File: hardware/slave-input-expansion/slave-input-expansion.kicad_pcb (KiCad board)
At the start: 2 copper layers, 78 parts, among them J1 Screw_Terminal_01x02, J10 Screw_Terminal_01x02, J11 Conn_01x06, J12 ICSP, J2 Screw_Terminal_01x02, J3 Screw_Terminal_01x02, J4 Screw_Terminal_01x02, J5 Screw_Terminal_01x02, J6 Screw_Terminal_01x02, J7 Screw_Terminal_01x02, J8 Screw_Terminal_01x02, J9 Conn_02x06_Odd_Even, SW1 SW_Push, SW2 SW_Push, U1 PC817XI, U10 DS1233A-10, U11 ESP32, U12 LM2596S-3.3, U13 LM2596S-3.3, U14 AMS1117-5.0, U2 PC817XI, U3 PC817XI, U4 PC817XI, U5 PC817XI, U6 PC817XI, U7 PC817XI, U8 PC817XI, U9 PCF8574

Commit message: Diseño mecanico del ensamblaje
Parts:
- removed C2, C4, C5: 100nF, Capacitor_SMD:C_1206_3216Metric_Pad1.33x1.80mm_HandSolder
- removed C3: 1uF, Capacitor_SMD:C_1206_3216Metric_Pad1.33x1.80mm_HandSolder
- removed C6, C7: 470uF, libs:CAP_10x10_SMD_THT
- removed D1: ABS10, Diode_SMD:Diode_Bridge_Diotec_ABS
- removed D2: LED, LED_SMD:LED_1206_3216Metric
- removed D3, D4: SS14, Diode_SMD:D_SMA_Handsoldering
- removed JP1, JP10, JP11, JP2, JP3, JP4, JP5, JP6, JP7, JP8, JP9: SolderJumper_2_Open, Jumper:SolderJumper-2_P1.3mm_Open_RoundedPad1.0x1.5mm
- removed L1, L2: 68uH, libs:L_12x12mm_H8mm
- removed R10, R11, R12, R13, R14, R15, R16, R17, R18, R19, R20, R21, R22, R23, R24, R9: 10k, Resistor_SMD:R_1206_3216Metric
- removed R25: 4K7, Resistor_SMD:R_1206_3216Metric
- removed R26: 5.6K, Resistor_THT:R_Axial_DIN0204_L3.6mm_D1.6mm_P2.54mm_Vertical
- removed R27: 12K, Resistor_THT:R_Axial_DIN0204_L3.6mm_D1.6mm_P2.54mm_Vertical
- removed SW1, SW2: SW_Push, Button_Switch_THT:SW_PUSH_6mm
- removed U10: DS1233A-10, Package_TO_SOT_THT:TO-92
- removed U12, U13: LM2596S-3.3, libs:TO-263-5_TabPin3
- removed U14: AMS1117-5.0, Package_TO_SOT_SMD:SOT-223-3_TabPin2
- removed U9: PCF8574, Package_SO:SOIC-16W_7.5x10.3mm_P1.27mm
- moved J11 84.2 mm to (181.6, 124.5)
- moved U11 81.8 mm to (184.2, 109.2), turned to -90 degrees
- moved J12 78.8 mm to (164.3, 124.5), turned to 90 degrees
- moved locked 69.0 mm to (188.0, 91.4), turned to 180 degrees
- moved R3 65.7 mm to (137.2, 97.8), turned to 180 degrees
- moved U3 65.1 mm to (124.5, 105.4), turned to -90 degrees
- moved locked 54.1 mm to (116.8, 91.4), turned to 180 degrees
- moved R1 53.4 mm to (116.8, 97.8), turned to 180 degrees
- moved R8 51.5 mm to (188.0, 97.8), turned to 180 degrees
- moved R7 50.2 mm to (177.8, 97.8), turned to 180 degrees
- moved locked 50.0 mm to (177.8, 91.4), turned to 180 degrees
- moved U7 49.7 mm to (149.9, 105.4), turned to -90 degrees
- moved J9 47.9 mm to (139.2, 116.8), turned to 90 degrees
- moved U8 46.3 mm to (156.2, 105.4), turned to -90 degrees
- moved U6 44.1 mm to (143.5, 105.4), turned to -90 degrees
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- renumbered J8 to locked, J1 to locked, J4 to locked, J2 to locked, J7 to locked, J5 to locked, J3 to locked, J6 to locked
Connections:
- R1 pad 2: Net-(J1-Pad1) -> Net-(R1-Pad2)
- R2 pad 2: Net-(J2-Pad1) -> Net-(R2-Pad2)
- R3 pad 2: Net-(J3-Pad1) -> Net-(R3-Pad2)
- R4 pad 2: Net-(J4-Pad1) -> Net-(R4-Pad2)
- R5 pad 2: Net-(J5-Pad1) -> Net-(R5-Pad2)
- R6 pad 2: Net-(J6-Pad1) -> Net-(J6-Pad2)
- R7 pad 2: Net-(J7-Pad1) -> Net-(R7-Pad2)
- R8 pad 2: Net-(J8-Pad1) -> Net-(R8-Pad2)
- U1 pad 2: Net-(J1-Pad2) -> Net-(U1-Pad2)
- U2 pad 2: Net-(J2-Pad2) -> Net-(U2-Pad2)
- U3 pad 2: Net-(J3-Pad2) -> Net-(U3-Pad2)
- U4 pad 2: Net-(J4-Pad2) -> Net-(U4-Pad2)
- U5 pad 2: Net-(J5-Pad2) -> Net-(U5-Pad2)
- U6 pad 2: Net-(J6-Pad2) -> Net-(U6-Pad2)
- U7 pad 2: Net-(J7-Pad2) -> Net-(U7-Pad2)
- U8 pad 2: Net-(J8-Pad2) -> Net-(U8-Pad2)
- locked pad 1: Net-(J8-Pad1) -> Net-(U8-Pad2)
- locked pad 2: Net-(J8-Pad2) -> Net-(R8-Pad2)
- locked pad 1: Net-(J1-Pad1) -> Net-(U1-Pad2)
- locked pad 2: Net-(J1-Pad2) -> Net-(R1-Pad2)
- locked pad 1: Net-(J4-Pad1) -> Net-(U4-Pad2)
- locked pad 2: Net-(J4-Pad2) -> Net-(R4-Pad2)
- locked pad 1: Net-(J2-Pad1) -> Net-(U2-Pad2)
- locked pad 2: Net-(J2-Pad2) -> Net-(R2-Pad2)
- locked pad 1: Net-(J7-Pad1) -> Net-(U7-Pad2)
- locked pad 2: Net-(J7-Pad2) -> Net-(R7-Pad2)
- locked pad 1: Net-(J5-Pad1) -> Net-(U5-Pad2)
- locked pad 2: Net-(J5-Pad2) -> Net-(R5-Pad2)
- locked pad 1: Net-(J3-Pad1) -> Net-(U3-Pad2)
- locked pad 2: Net-(J3-Pad2) -> Net-(R3-Pad2)
- locked pad 1: Net-(J6-Pad1) -> Net-(U6-Pad2)
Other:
- board outline added: 100 x 43 mm

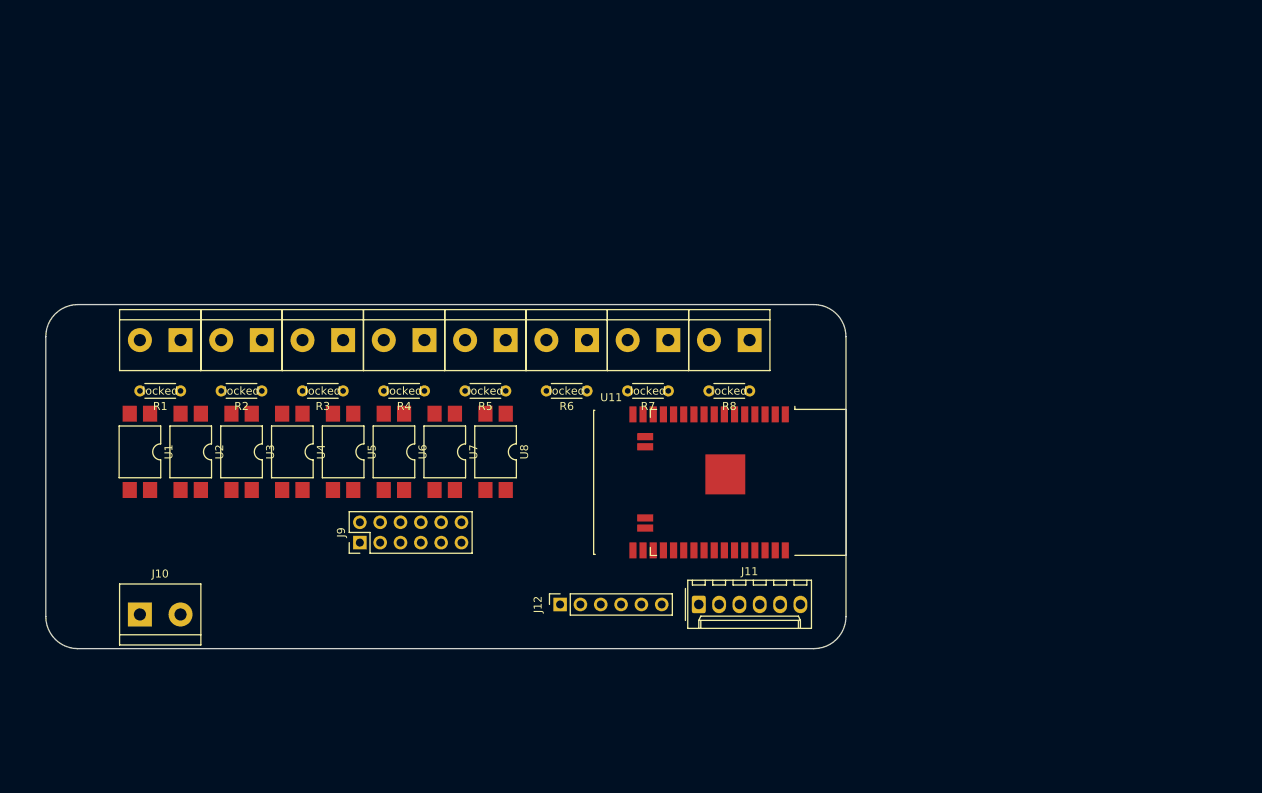
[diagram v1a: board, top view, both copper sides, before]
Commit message: Routeo de la placa expansion
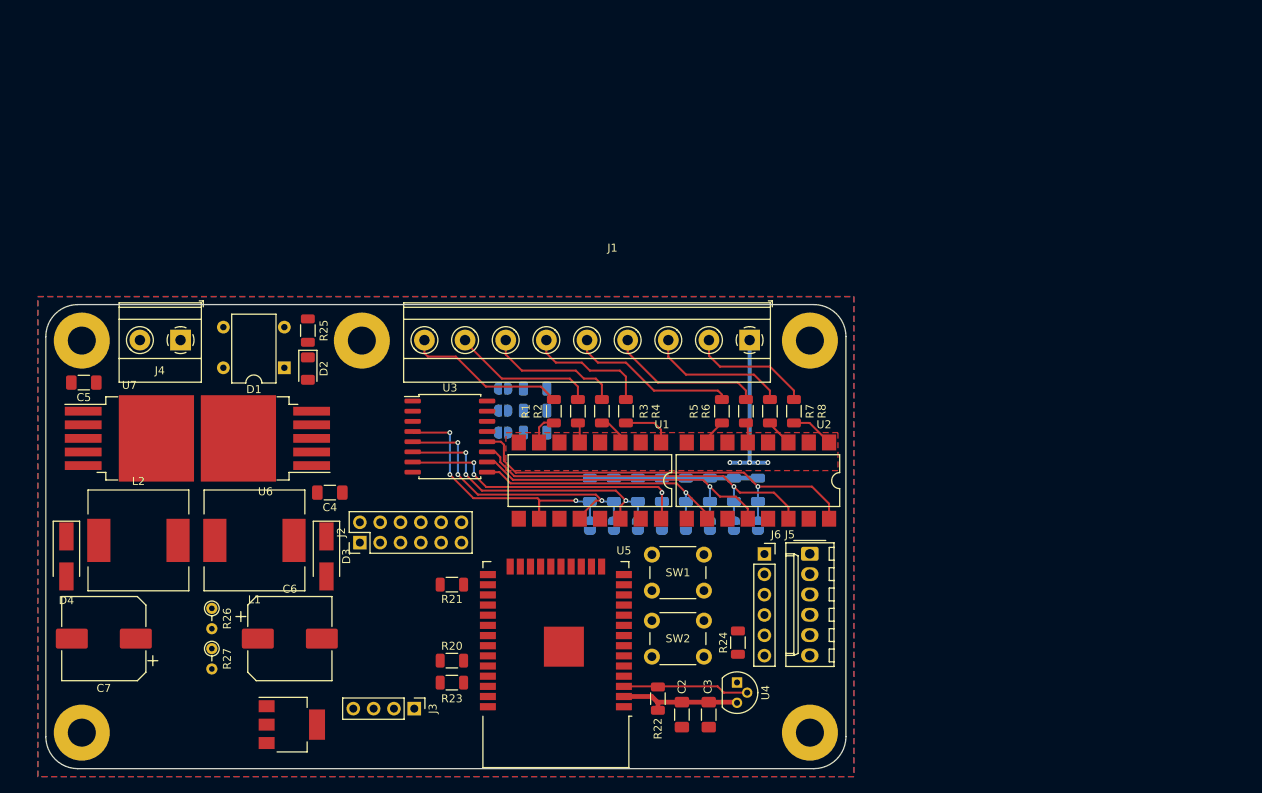
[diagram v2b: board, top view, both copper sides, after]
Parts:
- removed the U5 at (137.2, 105.4)
- removed locked (x8): Screw_Terminal_01x02, libs:TerminalBlock_bornier-2_P5.08mm
- added ?: , , F.Cu at (195.5, 140.5)
- added ?: , , F.Cu at (139.5, 91.5)
- added ?: , , F.Cu at (104.5, 91.5)
- added ?: , , F.Cu at (104.5, 140.5)
- added C2: 100nF, Capacitor_SMD:C_1206_3216Metric_Pad1.33x1.80mm_HandSolder, F.Cu at (179.5, 138.2)
- added C3: 1uF, Capacitor_SMD:C_1206_3216Metric_Pad1.33x1.80mm_HandSolder, F.Cu at (182.8, 138.2)
- added C4: 100nF, Capacitor_SMD:C_1206_3216Metric_Pad1.33x1.80mm_HandSolder, F.Cu at (135.5, 110.5)
- added C5: 100nF, Capacitor_SMD:C_1206_3216Metric_Pad1.33x1.80mm_HandSolder, F.Cu at (104.8, 96.8)
- added C6: 470uF, Capacitor_SMD:CP_Elec_10x10, F.Cu at (130.5, 128.8)
- added C7: 470uF, Capacitor_SMD:CP_Elec_10x10, F.Cu at (107.2, 128.8)
- added D1: DB157, Diode_THT:Diode_Bridge_DIP-4_W7.62mm_P5.08mm, F.Cu at (129.8, 94.9)
- added D2: LED, LED_SMD:LED_1206_3216Metric, F.Cu at (132.8, 95.0)
- added D3: SS14, Diode_SMD:D_SMA_Handsoldering, F.Cu at (135.1, 118.5)
- added D4: SS14, Diode_SMD:D_SMA_Handsoldering, F.Cu at (102.6, 118.5)
- added J1: Screw_Terminal_01x09, TerminalBlock_Phoenix:TerminalBlock_Phoenix_MKDS-1,5-9-5.08_1x09_P5.08mm_Horizontal, F.Cu at (188.0, 91.4)
- added J3: Conn_01x04, Connector_PinHeader_2.54mm:PinHeader_1x04_P2.54mm_Vertical, F.Cu at (146.1, 137.5)
- added JP1: SolderJumper_2_Open, Jumper:SolderJumper-2_P1.3mm_Open_RoundedPad1.0x1.5mm, B.Cu at (168.0, 114.7)
- added JP10: SolderJumper_2_Open, Jumper:SolderJumper-2_P1.3mm_Open_RoundedPad1.0x1.5mm, B.Cu at (157.2, 100.2)
- added JP11: SolderJumper_2_Open, Jumper:SolderJumper-2_P1.3mm_Open_RoundedPad1.0x1.5mm, B.Cu at (157.2, 103.0)
- added JP2: SolderJumper_2_Open, Jumper:SolderJumper-2_P1.3mm_Open_RoundedPad1.0x1.5mm, B.Cu at (171.0, 114.7)
- added JP3: SolderJumper_2_Open, Jumper:SolderJumper-2_P1.3mm_Open_RoundedPad1.0x1.5mm, B.Cu at (174.0, 114.7)
- added JP4: SolderJumper_2_Open, Jumper:SolderJumper-2_P1.3mm_Open_RoundedPad1.0x1.5mm, B.Cu at (177.0, 114.7)
- added JP5: SolderJumper_2_Open, Jumper:SolderJumper-2_P1.3mm_Open_RoundedPad1.0x1.5mm, B.Cu at (180.0, 114.7)
- added JP6: SolderJumper_2_Open, Jumper:SolderJumper-2_P1.3mm_Open_RoundedPad1.0x1.5mm, B.Cu at (183.0, 114.7)
- added JP7: SolderJumper_2_Open, Jumper:SolderJumper-2_P1.3mm_Open_RoundedPad1.0x1.5mm, B.Cu at (186.0, 114.7)
- added JP8: SolderJumper_2_Open, Jumper:SolderJumper-2_P1.3mm_Open_RoundedPad1.0x1.5mm, B.Cu at (189.0, 114.7)
- added JP9: SolderJumper_2_Open, Jumper:SolderJumper-2_P1.3mm_Open_RoundedPad1.0x1.5mm, B.Cu at (157.2, 97.5)
- added L1: 68uH, Inductor_SMD:L_12x12mm_H8mm, F.Cu at (126.1, 116.5)
- added L2: 68uH, Inductor_SMD:L_12x12mm_H8mm, F.Cu at (111.6, 116.5)
- added R10: 10k, Resistor_SMD:R_1206_3216Metric, B.Cu at (171.0, 110.2)
- added R11: 10k, Resistor_SMD:R_1206_3216Metric, B.Cu at (174.0, 110.2)
- added R12: 10k, Resistor_SMD:R_1206_3216Metric, B.Cu at (177.0, 110.2)
- added R13: 10k, Resistor_SMD:R_1206_3216Metric, B.Cu at (180.0, 110.2)
- added R14: 10k, Resistor_SMD:R_1206_3216Metric, B.Cu at (183.0, 110.2)
- added R15: 10k, Resistor_SMD:R_1206_3216Metric, B.Cu at (186.0, 110.2)
- added R16: 10k, Resistor_SMD:R_1206_3216Metric, B.Cu at (189.0, 110.2)
- added R17: 10k, Resistor_SMD:R_1206_3216Metric, B.Cu at (161.2, 103.0)
- added R18: 10k, Resistor_SMD:R_1206_3216Metric, B.Cu at (161.2, 100.2)
- added R19: 10k, Resistor_SMD:R_1206_3216Metric, B.Cu at (161.2, 97.5)
- added R20: 10k, Resistor_SMD:R_1206_3216Metric, F.Cu at (150.8, 131.5)
- added R21: 10k, Resistor_SMD:R_1206_3216Metric, F.Cu at (150.8, 122.0)
- added R22: 10k, Resistor_SMD:R_1206_3216Metric, F.Cu at (176.5, 136.2)
- added R23: 10k, Resistor_SMD:R_1206_3216Metric, F.Cu at (150.8, 134.2)
- added R24: 10k, Resistor_SMD:R_1206_3216Metric, F.Cu at (186.5, 129.2)
- added R25: 4K7, Resistor_SMD:R_1206_3216Metric, F.Cu at (132.8, 90.2)
- added R26: 5.6K, Resistor_THT:R_Axial_DIN0204_L3.6mm_D1.6mm_P2.54mm_Vertical, F.Cu at (120.8, 125.0)
- added R27: 12K, Resistor_THT:R_Axial_DIN0204_L3.6mm_D1.6mm_P2.54mm_Vertical, F.Cu at (120.8, 130.0)
- added R9: 10k, Resistor_SMD:R_1206_3216Metric, B.Cu at (168.0, 110.2)
- added REF**: MountingHole_3.5mm_Pad, MountingHole:MountingHole_3.5mm_Pad, F.Cu at (195.5, 91.5)
- added SW1: SW_Push, Button_Switch_THT:SW_PUSH_6mm, F.Cu at (182.2, 122.8)
- added SW2: SW_Push, Button_Switch_THT:SW_PUSH_6mm, F.Cu at (182.2, 131.0)
- J4: renamed from J10; footprint libs:TerminalBlock_bornier-2_P5.08mm -> TerminalBlock_Phoenix:TerminalBlock_Phoenix_MKDS-1,5-2-5.08_1x02_P5.08mm_Horizontal
- R1, R2, R3, R4, R5, R6, R7, R8: value 2.2k -> 1k; footprint Resistor_THT:R_Axial_DIN0204_L3.6mm_D1.6mm_P5.08mm_Horizontal -> Resistor_SMD:R_1206_3216Metric
- U1, U2: value PC817XI -> LTV-847S; footprint Package_DIP:SMDIP-4_W9.53mm -> Package_DIP:SMDIP-16_W9.53mm
- U3: value PC817XI -> PCF8574; footprint Package_DIP:SMDIP-4_W9.53mm -> Package_SO:SOIC-16W_7.5x10.3mm_P1.27mm
- U4: value PC817XI -> DS1233A-10; footprint Package_DIP:SMDIP-4_W9.53mm -> Package_TO_SOT_THT:TO-92
- U5: renamed from U11; footprint esp32-wroom-roover:ESP32-WROOM-WROVER-NC -> esp32-wroom-roover:ESP32-WROOM-32
- U6, U7: value PC817XI -> LM2596S-3.3; footprint Package_DIP:SMDIP-4_W9.53mm -> Package_TO_SOT_SMD:TO-263-5_TabPin3
- U8: value PC817XI -> AMS1117-5.0; footprint Package_DIP:SMDIP-4_W9.53mm -> Package_TO_SOT_SMD:SOT-223-3_TabPin2
- moved U2 71.0 mm to (189.0, 109.0)
- moved U4 62.6 mm to (186.4, 134.2)
- moved U1 56.4 mm to (168.0, 109.0)
- moved R1 46.7 mm to (163.5, 100.3), turned to -90 degrees
- moved U8 42.5 mm to (130.8, 139.5), turned to 0 degrees
- moved R2 39.6 mm to (166.5, 100.3), turned to -90 degrees
- moved U7 39.4 mm to (110.5, 103.7), turned to 0 degrees
- moved J4 34.7 mm to (116.8, 91.4), turned to 180 degrees
- moved R3 32.4 mm to (169.5, 100.3), turned to -90 degrees
- moved U5 28.4 mm to (163.8, 129.0), turned to 180 degrees
- moved R5 27.1 mm to (184.5, 100.3), turned to -90 degrees
- moved J6 26.3 mm to (189.8, 118.2), turned to 0 degrees
- moved U3 26.1 mm to (150.5, 103.5), turned to 0 degrees
- moved R4 25.3 mm to (172.5, 100.3), turned to -90 degrees
- moved R6 20.0 mm to (187.5, 100.3), turned to -90 degrees
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- renumbered J9 to J2, J11 to J5, J12 to J6
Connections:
- R1 pad 1: Net-(R1-Pad1) -> Net-(J1-Pad9)
- R2 pad 1: Net-(R2-Pad1) -> Net-(J1-Pad8)
- R3 pad 1: Net-(R3-Pad1) -> Net-(J1-Pad7)
- R4 pad 1: Net-(R4-Pad1) -> Net-(J1-Pad6)
- R6 pad 1: Net-(R6-Pad1) -> Net-(J1-Pad4)
- R6 pad 2: Net-(J6-Pad2) -> Net-(R6-Pad2)
- R7 pad 1: Net-(R7-Pad1) -> Net-(J1-Pad3)
- R8 pad 1: Net-(R8-Pad1) -> Net-(J1-Pad2)
- U1 pad 1: Net-(R1-Pad1) -> Net-(R4-Pad2)
- U1 pad 2: Net-(U1-Pad2) -> Net-(J1-Pad1)
- U1 pad 3: GND -> Net-(R3-Pad2)
- U1 pad 4: IN0 -> Net-(J1-Pad1)
- U2 pad 1: Net-(R2-Pad1) -> Net-(R8-Pad2)
- U2 pad 2: Net-(U2-Pad2) -> Net-(J1-Pad1)
- U2 pad 3: GND -> Net-(R7-Pad2)
- U2 pad 4: IN1 -> Net-(J1-Pad1)
- U3 pad 1: Net-(R3-Pad1) -> Net-(JP9-Pad2)
- U3 pad 3: GND -> Net-(JP11-Pad2)
- U3 pad 4: IN2 -> IN0
- U4 pad 1: Net-(R4-Pad1) -> GND
- U4 pad 2: Net-(U4-Pad2) -> RESET
- U4 pad 3: GND -> +3V3
- U6 pad 1: Net-(R6-Pad1) -> /Power Supply/VIN
- U6 pad 4: IN5 -> Net-(R26-Pad1)
- U7 pad 1: Net-(R7-Pad1) -> /Power Supply/VIN
- U7 pad 4: IN6 -> +3V3
- U8 pad 1: Net-(R8-Pad1) -> GND
- U8 pad 2: Net-(U8-Pad2) -> +5V
- U8 pad 3: GND -> +12V
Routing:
- net IN7: track 0.00 -> 53.2 mm, vias 0 -> 1
- net IN6: track 0.00 -> 46.6 mm, vias 0 -> 1
- net IN3: track 0.00 -> 40.6 mm, vias 0 -> 3
- net IN5: track 0.00 -> 40.5 mm, vias 0 -> 1
- net IN2: track 0.00 -> 37.3 mm, vias 0 -> 3
- net IN1: track 0.00 -> 36.8 mm, vias 0 -> 3
- net +3V3: track 0.00 -> 36.5 mm
- net IN0: track 0.00 -> 35.8 mm, vias 0 -> 3
- net IN4: track 0.00 -> 33.8 mm, vias 0 -> 1
- net Net-(J1-Pad5): track 0.00 -> 21.1 mm
- net Net-(J1-Pad9): track 0.00 -> 20.2 mm
- net Net-(J1-Pad1): track 0.00 -> 20.1 mm, vias 0 -> 5
- net Net-(J1-Pad4): track 0.00 -> 19.4 mm
- net Net-(J1-Pad8): track 0.00 -> 18.2 mm
- net Net-(J1-Pad3): track 0.00 -> 17.7 mm
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- added copper zone on B.Cu, net GND
- added copper zone on F.Cu, net GND
- added copper zone on F.Cu, net Net-(J1-Pad1)
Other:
- board size 100 x 43 mm -> 100 x 58 mm
